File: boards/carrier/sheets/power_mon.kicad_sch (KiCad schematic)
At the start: 2 parts, among them U1 INA226AIDGSR

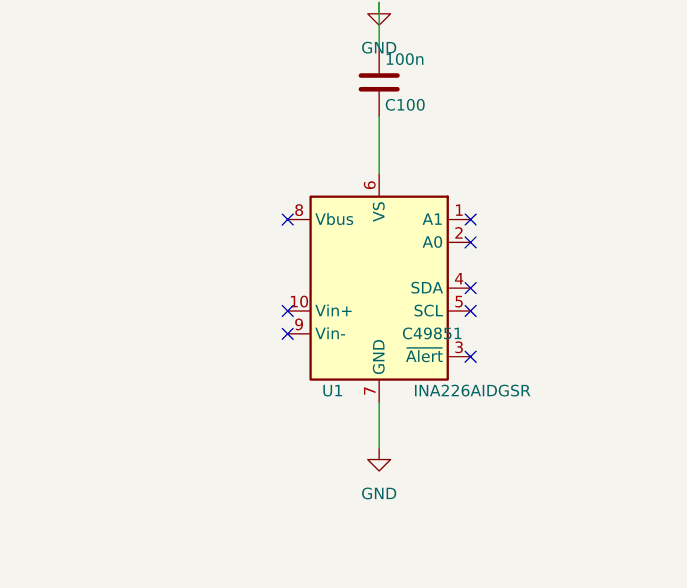
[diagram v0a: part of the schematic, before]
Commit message: carrier: regenerate after Tracks 2a + 2c merge
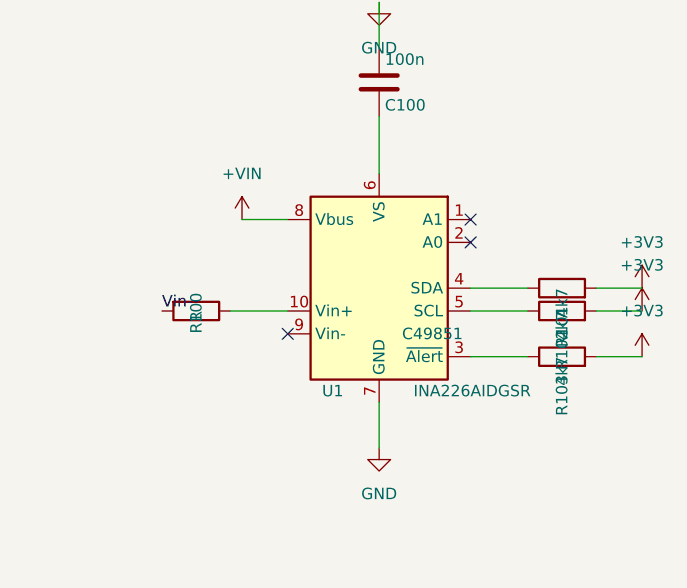
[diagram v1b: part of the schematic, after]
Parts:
- added R100: R, Resistor_SMD:R_0402_1005Metric, symbol Device:R
- added R101, R102, R103: 4k7, Resistor_SMD:R_0402_1005Metric, symbol Device:R
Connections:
- net at U1.10 (Vin+): now also R100.1
- net at U1.3 (~{Alert}): now also R103.1
- net at U1.4 (SDA): now also R101.1
- net at U1.5 (SCL): now also R102.1
- net +VIN: now reaches U1.8 (Vbus)
- new net +3V3: R101.2, R102.2, R103.2
- new net Vin-: R100.2
- no-connect marks 8 -> 3
